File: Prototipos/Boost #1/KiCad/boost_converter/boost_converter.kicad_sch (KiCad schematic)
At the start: 15 parts, among them J1 Screw_Terminal_01x02, J2 Screw_Terminal_01x02, Q1 NMOS

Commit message: Agregado de driver de mosfet
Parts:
- added C6: 10u, Capacitor_THT:C_Disc_D3.8mm_W2.6mm_P2.50mm, symbol Device:C_Small
- added C7: 65p, Capacitor_THT:C_Disc_D3.8mm_W2.6mm_P2.50mm, symbol Device:C_Small
- added C8: ~, Capacitor_THT:C_Disc_D3.8mm_W2.6mm_P2.50mm, symbol Device:C_Small
- added D4, D5: D_Schottky, Diode_THT:D_A-405_P10.16mm_Horizontal, symbol Device:D_Schottky_Small
- added Q2: NPN, symbol Simulation_SPICE:NPN
- added Q3: IRLML6344, IRLML6344:SOT23, symbol IRLML6344:IRLML6344
- added R10, R11: 150, Resistor_THT:R_Axial_DIN0207_L6.3mm_D2.5mm_P15.24mm_Horizontal, symbol Device:R_Small
- added R12: 100, Resistor_THT:R_Axial_DIN0207_L6.3mm_D2.5mm_P15.24mm_Horizontal, symbol Device:R_Small
- added R13, R17: 1k, Resistor_THT:R_Axial_DIN0207_L6.3mm_D2.5mm_P15.24mm_Horizontal, symbol Device:R_Small
- added R14: 27, Resistor_THT:R_Axial_DIN0207_L6.3mm_D2.5mm_P15.24mm_Horizontal, symbol Device:R_Small
- added R15, R16, R18: ~, Resistor_THT:R_Axial_DIN0207_L6.3mm_D2.5mm_P15.24mm_Horizontal, symbol Device:R_Small
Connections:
- net Retro: now also C6.1, R10.2; no longer R4.2, R5.1
- net 12V: now reaches C1.1, J1.2 (Pin_2), L1.1
- net 12V: now also R12.1, R16.1
- net at C1.2, C2.2, C4.2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: now also C6.2
- net PWM renamed Gate
- net Gate: now also D4.1 (K), D5.1 (K), Q2.1 (C), Q3.3, R12.2, R14.1, R16.2, R18.1
- new net: Q2.2 (B), R15.2, R17.1
- new net: Q3.1, R11.2, R13.1
- new net: C8.1, R18.2
- new net: R10.1, R4.2, R5.1
- new net: C7.1, R14.2
- new net PGND: C7.2, C8.2, D4.2 (A), D5.2 (A), Q2.3 (E), Q3.2, R13.2, R17.2
- new net PWM_micro: R11.1, R15.1
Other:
- note added: "Disparar MOSFET-p con BJT"
- note added: "Disparar MOSFET-p con MOSFET"
- moved on the sheet: J2

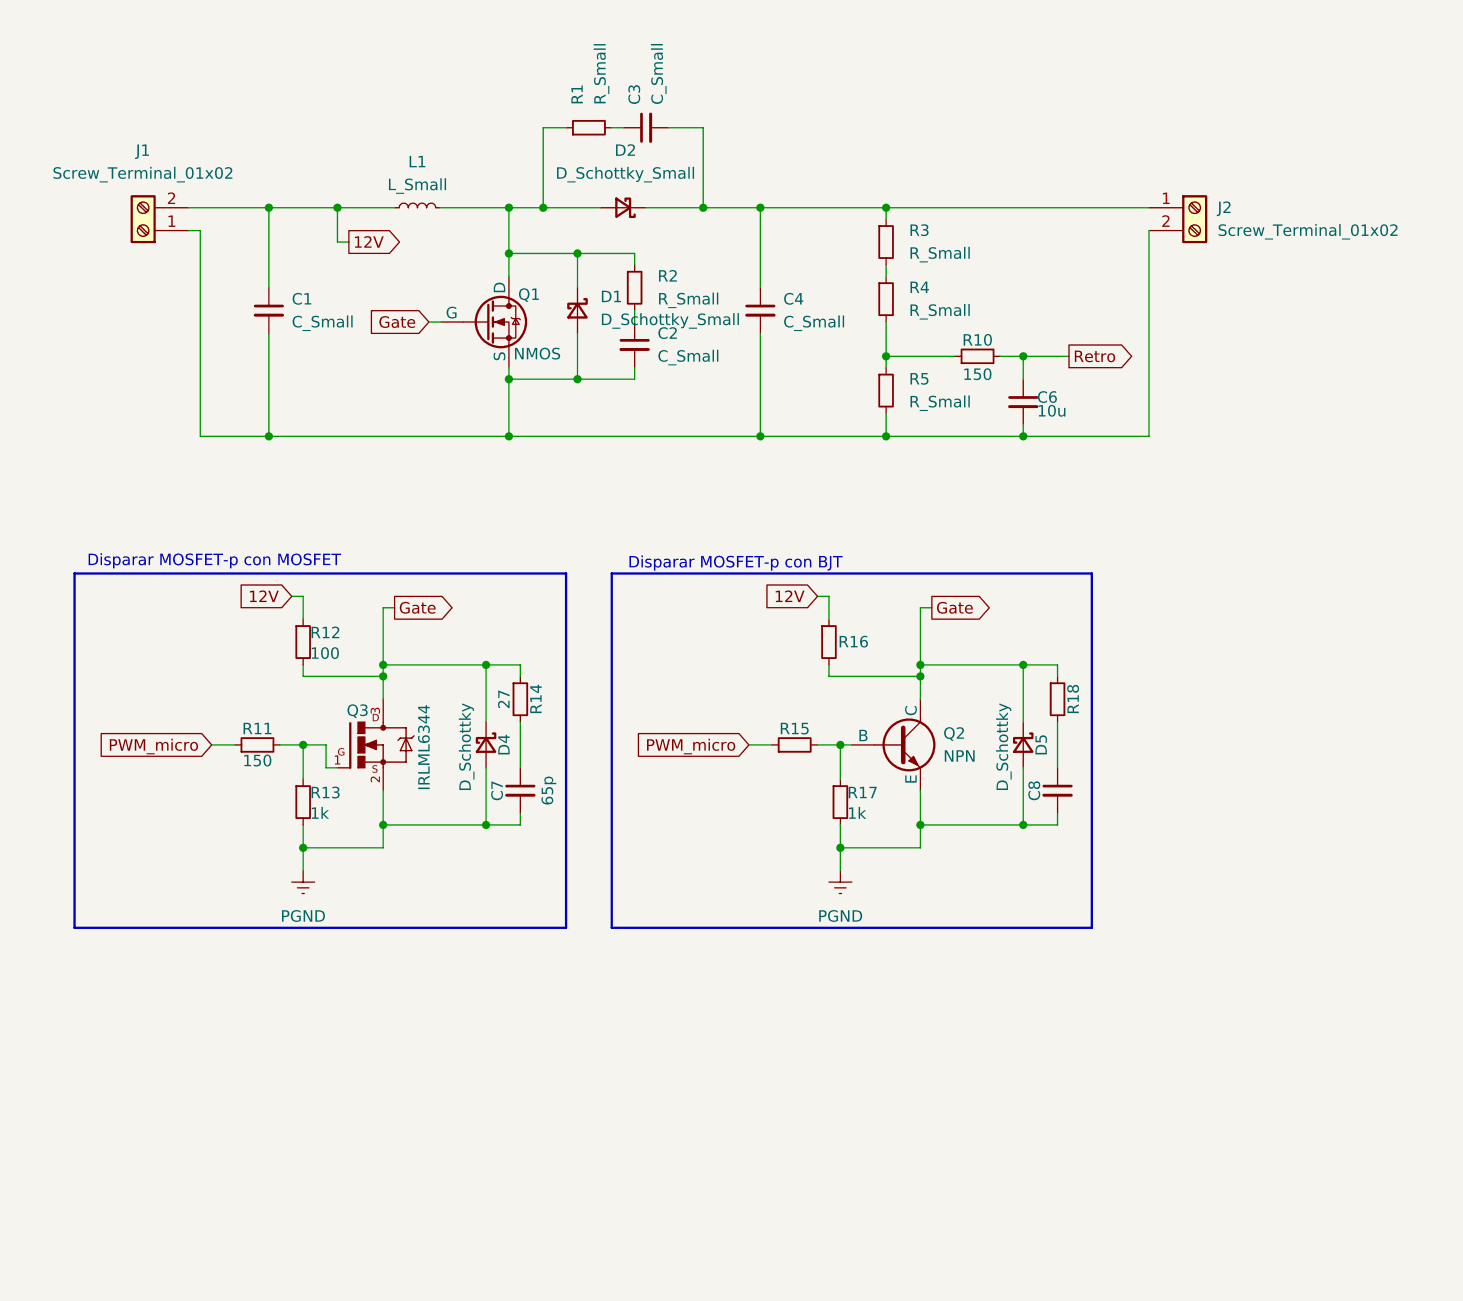
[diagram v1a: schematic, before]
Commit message: Diseño de circuito sin valores
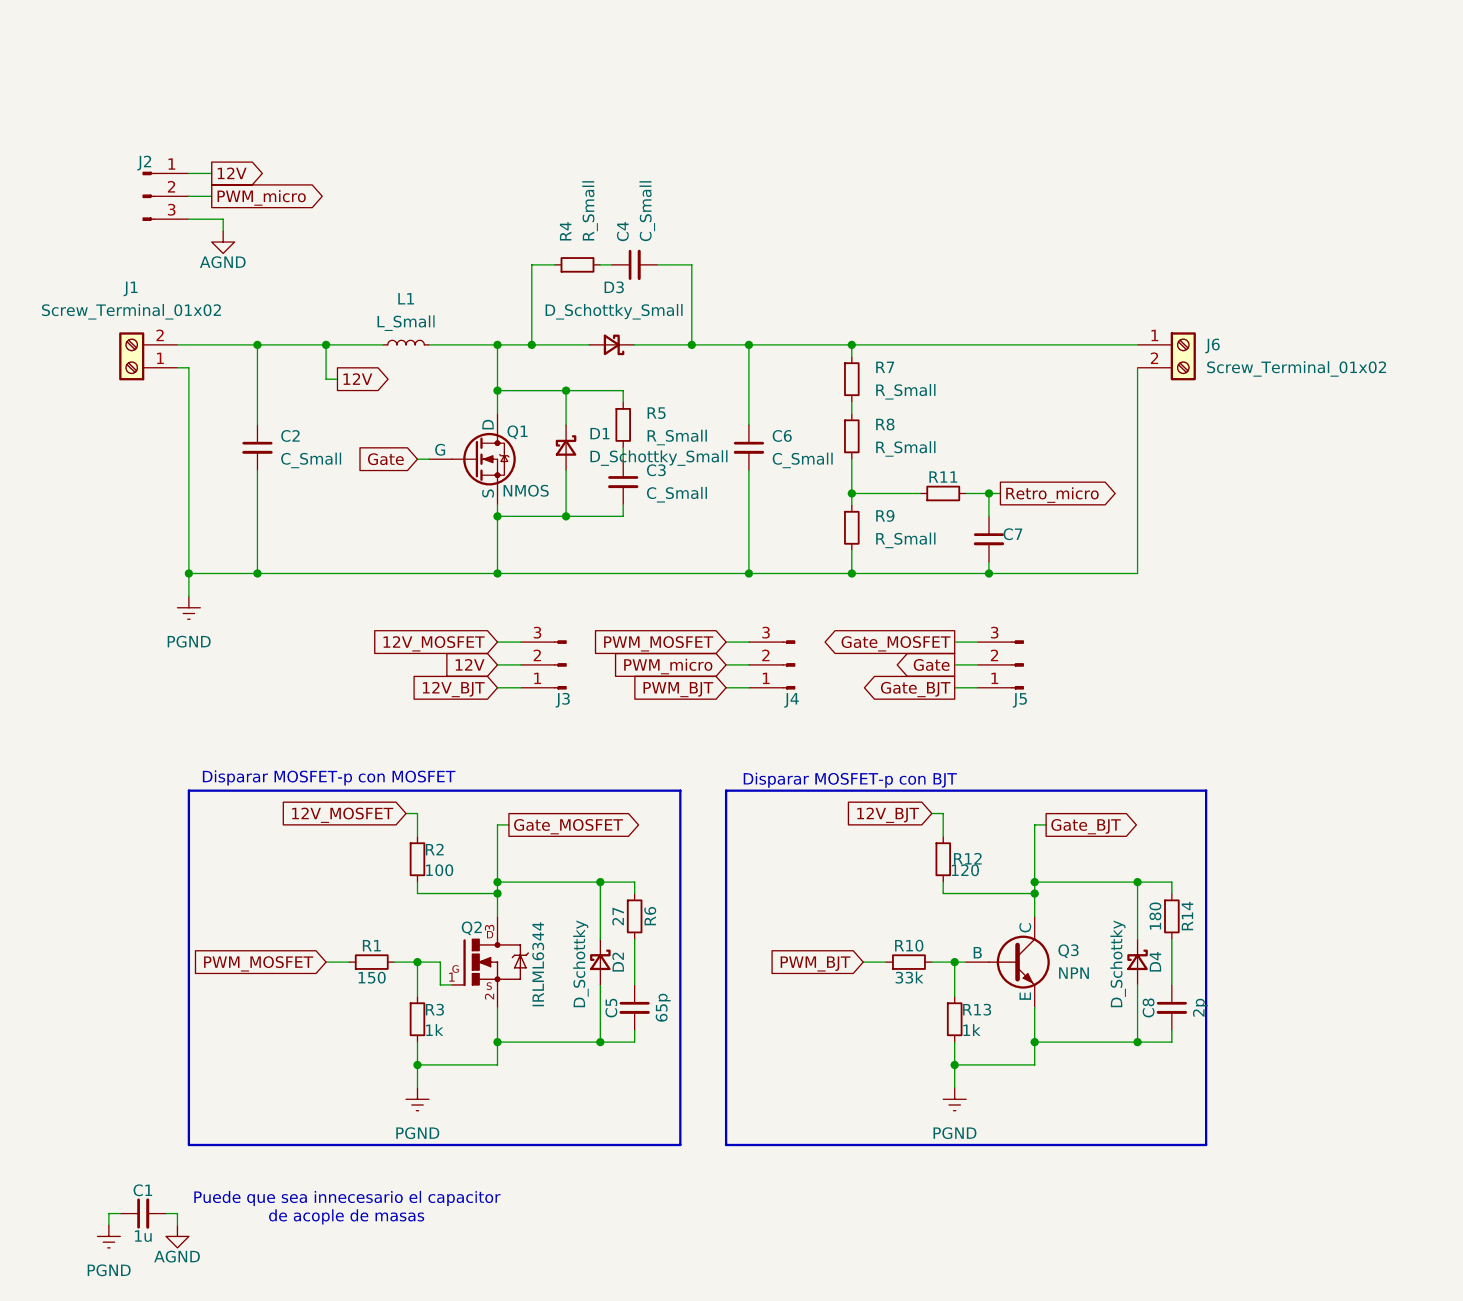
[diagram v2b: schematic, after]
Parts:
- removed C7: 65p, Capacitor_THT:C_Disc_D3.8mm_W2.6mm_P2.50mm, symbol Device:C_Small
- removed D5: D_Schottky, Diode_THT:D_A-405_P10.16mm_Horizontal, symbol Device:D_Schottky_Small
- removed Q2: NPN, symbol Simulation_SPICE:NPN
- removed Q3: IRLML6344, IRLML6344:SOT23, symbol IRLML6344:IRLML6344
- removed R11: 150, Resistor_THT:R_Axial_DIN0207_L6.3mm_D2.5mm_P15.24mm_Horizontal, symbol Device:R_Small
- removed R15, R16, R18: ~, Resistor_THT:R_Axial_DIN0207_L6.3mm_D2.5mm_P15.24mm_Horizontal, symbol Device:R_Small
- removed R17: 1k, Resistor_THT:R_Axial_DIN0207_L6.3mm_D2.5mm_P15.24mm_Horizontal, symbol Device:R_Small
- added C1: 1u, Capacitor_THT:C_Disc_D3.8mm_W2.6mm_P2.50mm, symbol Device:C_Small
- added C5: 65p, Capacitor_THT:C_Disc_D3.8mm_W2.6mm_P2.50mm, symbol Device:C_Small
- added D4: D_Schottky, Diode_THT:D_DO-34_SOD68_P7.62mm_Horizontal, symbol Device:D_Schottky_Small
- added J2, J3, J4, J5: Conn_01x03_Pin, Connector_PinHeader_2.54mm:PinHeader_1x03_P2.54mm_Vertical, symbol Connector:Conn_01x03_Pin
- added Q2: IRLML6344, KICAD-Libraries:SOT23, symbol IRLML6344:IRLML6344
- added Q3: NPN, Package_TO_SOT_THT:TO-92_Inline, symbol Simulation_SPICE:NPN
- added R1: 150, Resistor_THT:R_Axial_DIN0207_L6.3mm_D2.5mm_P7.62mm_Horizontal, symbol Device:R_Small
- added R10: 33k, Resistor_THT:R_Axial_DIN0207_L6.3mm_D2.5mm_P7.62mm_Horizontal, symbol Device:R_Small
- added R14: 180, Resistor_THT:R_Axial_DIN0207_L6.3mm_D2.5mm_P7.62mm_Horizontal, symbol Device:R_Small
- added R2: 100, Resistor_THT:R_Axial_DIN0207_L6.3mm_D2.5mm_P7.62mm_Horizontal, symbol Device:R_Small
- added R3: 1k, Resistor_THT:R_Axial_DIN0207_L6.3mm_D2.5mm_P7.62mm_Horizontal, symbol Device:R_Small
- C7: renamed from C6; value 10u -> ~
- C8: value ~ -> 2p
- D2: renamed from D4; footprint Diode_THT:D_A-405_P10.16mm_Horizontal -> Diode_THT:D_DO-34_SOD68_P7.62mm_Horizontal
- R11: renamed from R10; value 150 -> ~
- R12: value 100 -> 120; footprint Resistor_THT:R_Axial_DIN0207_L6.3mm_D2.5mm_P15.24mm_Horizontal -> Resistor_THT:R_Axial_DIN0207_L6.3mm_D2.5mm_P7.62mm_Horizontal
- R13: footprint Resistor_THT:R_Axial_DIN0207_L6.3mm_D2.5mm_P15.24mm_Horizontal -> Resistor_THT:R_Axial_DIN0207_L6.3mm_D2.5mm_P7.62mm_Horizontal
- R6: renamed from R14; footprint Resistor_THT:R_Axial_DIN0207_L6.3mm_D2.5mm_P15.24mm_Horizontal -> Resistor_THT:R_Axial_DIN0207_L6.3mm_D2.5mm_P7.62mm_Horizontal
- renumbered C1 to C2, C2 to C3, C3 to C4, C4 to C6, D2 to D3, J2 to J6, R1 to R4, R2 to R5, R3 to R7, R4 to R8, R5 to R9
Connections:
- net 12V: now also J2.1 (Pin_1), J3.2 (Pin_2); no longer R12.1
- net Gate: now also J5.2 (Pin_2); no longer D2.1 (K), R12.2, R6.1
- net PGND: now also C2.2, C3.2, C6.2, C7.2, D1.2 (A), J1.1 (Pin_1), J6.2 (Pin_2), Q1.3 (S), R9.2, C1.1, C5.2, D4.2 (A), Q2.2, Q3.3 (E), R3.2
- net PWM_micro: now also J2.2 (Pin_2), J4.2 (Pin_2)
- net at R13.1: now also Q3.2 (B), R10.2
- net at C8.1: now also R14.2
- net at R6.2: now also C5.1
- net Retro renamed Retro_micro
- new net: Q2.1, R1.2, R3.1
- new net 12V_BJT: J3.1 (Pin_1), R12.1
- new net 12V_MOSFET: J3.3 (Pin_3), R2.1
- new net AGND: C1.2, J2.3 (Pin_3)
- new net Gate_BJT: D4.1 (K), J5.1 (Pin_1), Q3.1 (C), R12.2, R14.1
- new net Gate_MOSFET: D2.1 (K), J5.3 (Pin_3), Q2.3, R2.2, R6.1
- new net PWM_BJT: J4.1 (Pin_1), R10.1
- new net PWM_MOSFET: J4.3 (Pin_3), R1.1
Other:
- note added: "Puede que sea innecesario el capacitor de acople de masas"
- moved on the sheet: C2, C3, C4, C6, C7, D1, D2, D3, J1, J6, L1, Q1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
